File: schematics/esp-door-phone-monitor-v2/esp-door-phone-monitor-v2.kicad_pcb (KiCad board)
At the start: 2 copper layers, 56.8 x 25.7 mm, 47 parts, among them J1 PHONE, J2 PWR_IN, J3 PROGRAM, K1 D3204, Q1 SS8050-G, Q2 SS8050-G, Q3 AO3480, U1 OP07, U2 AMS1117-3.3, U3 ESP-12E

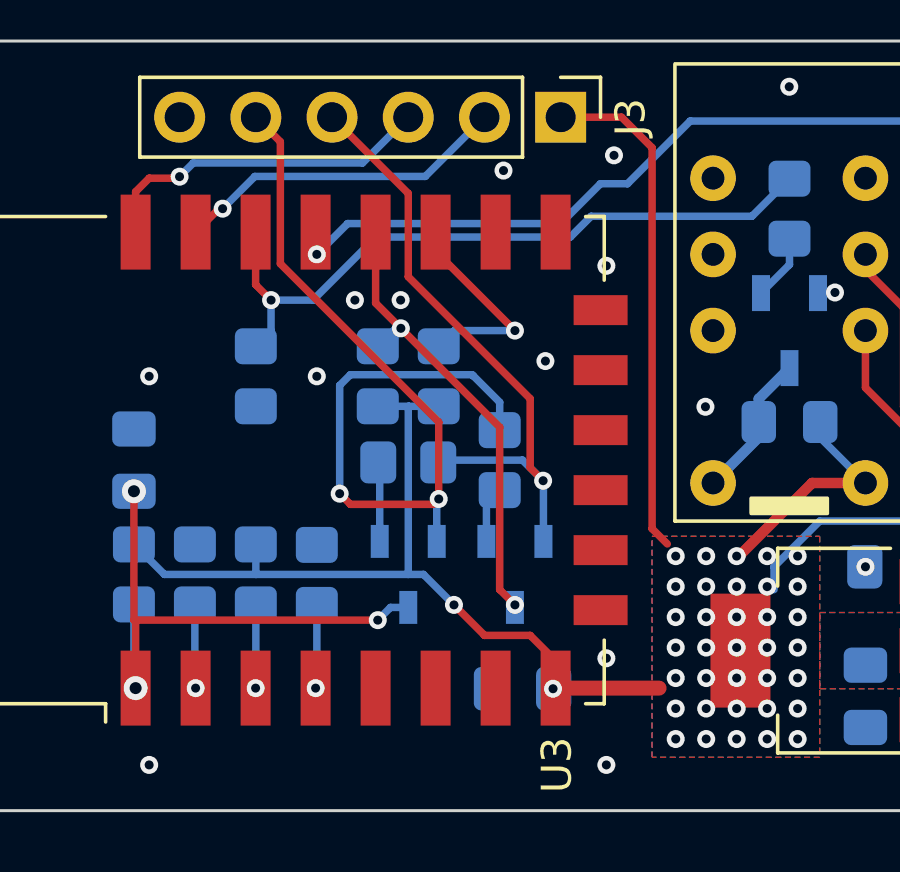
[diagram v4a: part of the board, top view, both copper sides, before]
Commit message: Fix pull-down resistor on GPIO15
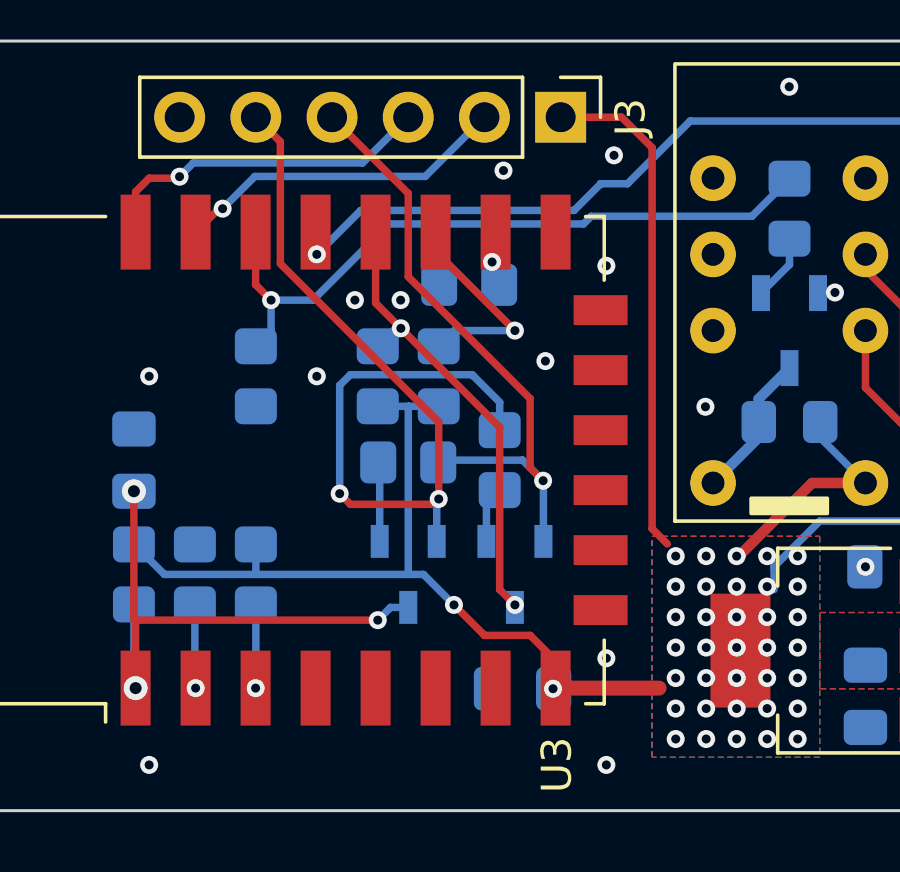
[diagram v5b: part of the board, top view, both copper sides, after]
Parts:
- moved R7 10.9 mm to (128.5, 93.0), turned to 180 degrees
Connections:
- U3 pad 16: unconnected-(U3-Pad16) -> Net-(R7-Pad1)
- U3 pad 4: Net-(R7-Pad1) -> unconnected-(U3-Pad4)
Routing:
- net Net-(R7-Pad1): track 2.79 -> 0.86 mm
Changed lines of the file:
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@@
   (net 19 "unconnected-(U3-Pad13)")
   (net 20 "unconnected-(U3-Pad14)")
-  (net 21 "unconnected-(U3-Pad16)")
+  (net 21 "unconnected-(U3-Pad4)")
   (net 22 "ESP_RINGING_SENSE")
   (net 23 "ESP_MUTE_CTRL")
@@
       (net 7 "ESP_EN") (pinfunction "EN") (pintype "input"))
     (pad "4" smd rect locked (at -7.6 2.5 90) (size 2.5 1) (layers "F.Cu" "F.Paste" "F.Mask")
-      (net 10 "Net-(R7-Pad1)") (pinfunction "GPIO16") (pintype "bidirectional"))
+      (net 21 "unconnected-(U3-Pad4)") (pinfunction "GPIO16") (pintype "bidirectional"))
     (pad "5" smd rect locked (at -7.6 4.5 90) (size 2.5 1) (layers "F.Cu" "F.Paste" "F.Mask")
       (net 12 "unconnected-(U3-Pad5)") (pinfunction "GPIO14") (pintype "bidirectional"))
@@
       (net 2 "GND") (pinfunction "GND") (pintype "power_in"))
     (pad "16" smd rect locked (at 7.6 8.5 90) (size 2.5 1) (layers "F.Cu" "F.Paste" "F.Mask")
-      (net 21 "unconnected-(U3-Pad16)") (pinfunction "GPIO15") (pintype "bidirectional"))
+      (net 10 "Net-(R7-Pad1)") (pinfunction "GPIO15") (pintype "bidirectional"))
     (pad "17" smd rect locked (at 7.6 6.5 90) (size 2.5 1) (layers "F.Cu" "F.Paste" "F.Mask")
       (net 11 "Net-(R8-Pad2)") (pinfunction "GPIO2") (pintype "bidirectional"))
@@
     (property "Sheetname" "")
     (attr smd)
-    (fp_text reference "R6" (at 3.556 0 90) (layer "B.SilkS")
+    (fp_text reference "R6" (at 1.27 -1.778 90) (layer "B.SilkS")
       (effects (font (size 1 1) (thickness 0.15)) (justify mirror))
     )
@@
     (property "Sheetname" "")
     (attr smd)
-    (fp_text reference "R8" (at 3.556 0 90) (layer "B.SilkS")
+    (fp_text reference "R8" (at 0.762 1.778 90) (layer "B.SilkS")
       (effects (font (size 1 1) (thickness 0.15)) (justify mirror))
     )
@@
   )
   (footprint "Resistor_SMD:R_0805_2012Metric_Pad1.20x1.40mm_HandSolder" (layer "B.Cu")
-    (at 123.444 102.632 90)
-    (descr "Resistor SMD 0805 (2012 Metric), square (rectangular) end terminal, IPC_7351 nominal with elongated pad for handsoldering. (Body size source: IPC-SM-782 page 72, https://www.pcb-3d.com/wordpress/wp-content/uploads/ipc-sm-782a_amendment_1_and_2.pdf), generated with kicad-footprint-generator")
-    (tags "resistor handsolder")
-    (property "Sheetfile" "esp-door-phone-monitor-v2.kicad_sch")
-    (property "Sheetname" "")
-    (attr smd)
-    (fp_text reference "R7" (at -2.778 0 90) (layer "B.SilkS")
-      (effects (font (size 1 1) (thickness 0.15)) (justify mirror))
-    )
-    (fp_text value "10k" (at 0 -1.65 90) (layer "B.Fab")
-      (effects (font (size 1 1) (thickness 0.15)) (justify mirror))
-    )
-    (fp_text user "${REFERENCE}" (at 0 0 90) (layer "B.Fab")
+    (at 128.524 92.964 180)
+    (descr "Resistor SMD 0805 (2012 Metric), square (rectangular) end terminal, IPC_7351 nominal with elongated pad for handsoldering. (Body size source: IPC-SM-782 page 72, https://www.pcb-3d.com/wordpress/wp-content/uploads/ipc-sm-782a_amendment_1_and_2.pdf), generated with kicad-footprint-generator")
+    (tags "resistor handsolder")
+    (property "Sheetfile" "esp-door-phone-monitor-v2.kicad_sch")
+    (property "Sheetname" "")
+    (attr smd)
+    (fp_text reference "R7" (at -3.048 0) (layer "B.SilkS")
+      (effects (font (size 1 1) (thickness 0.15)) (justify mirror))
+    )
+    (fp_text value "10k" (at 0 -1.65) (layer "B.Fab")
+      (effects (font (size 1 1) (thickness 0.15)) (justify mirror))
+    )
+    (fp_text user "${REFERENCE}" (at 0 0) (layer "B.Fab")
       (effects (font (size 0.5 0.5) (thickness 0.08)) (justify mirror))
     )
@@
     (fp_line (start 1 -0.625) (end -1 -0.625) (layer "B.Fab") (width 0.1))
     (fp_line (start 1 0.625) (end 1 -0.625) (layer "B.Fab") (width 0.1))
-    (pad "1" smd roundrect locked (at -1 0 90) (size 1.2 1.4) (layers "B.Cu" "B.Paste" "B.Mask") (roundrect_rratio 0.2083333333)
+    (pad "1" smd roundrect locked (at -1 0 180) (size 1.2 1.4) (layers "B.Cu" "B.Paste" "B.Mask") (roundrect_rratio 0.2083333333)
       (net 10 "Net-(R7-Pad1)") (pintype "passive"))
-    (pad "2" smd roundrect locked (at 1 0 90) (size 1.2 1.4) (layers "B.Cu" "B.Paste" "B.Mask") (roundrect_rratio 0.2083333333)
+    (pad "2" smd roundrect locked (at 1 0 180) (size 1.2 1.4) (layers "B.Cu" "B.Paste" "B.Mask") (roundrect_rratio 0.2083333333)
       (net 2 "GND") (pintype "passive"))
     (model "${KICAD6_3DMODEL_DIR}/Resistor_SMD.3dshapes/R_0805_2012Metric.wrl"
@@
   (segment (start 126.075625 94.412375) (end 125.476 95.012) (width 0.25) (layer "B.Cu") (net 9))
   (segment (start 126.246003 94.412375) (end 126.075625 94.412375) (width 0.25) (layer "B.Cu") (net 9))
-  (via (at 123.404 106.406) (size 0.6) (drill 0.3) (layers "F.Cu" "B.Cu") (net 10))
-  (segment (start 123.444 106.366) (end 123.404 106.406) (width 0.25) (layer "B.Cu") (net 10))
-  (segment (start 123.444 103.632) (end 123.444 106.366) (width 0.25) (layer "B.Cu") (net 10))
+  (via (at 129.286 92.202) (size 0.6) (drill 0.3) (layers "F.Cu" "B.Cu") (net 10))
+  (segment (start 129.524 92.964) (end 129.524 92.44) (width 0.25) (layer "B.Cu") (net 10))
+  (segment (start 129.524 92.44) (end 129.286 92.202) (width 0.25) (layer "B.Cu") (net 10))
   (segment (start 127.404 91.206) (end 127.404 91.844) (width 0.25) (layer "F.Cu") (net 11))
   (segment (start 127.404 91.844) (end 130.048 94.488) (width 0.25) (layer "F.Cu") (net 11))
@@
   (segment (start 130.048 94.488) (end 128.032 94.488) (width 0.25) (layer "B.Cu") (net 11))
   (via (at 123.444 91.948) (size 0.6) (drill 0.3) (layers "F.Cu" "B.Cu") (net 22))
+  (segment (start 132.898489 89.59348) (end 132.898489 89.605511) (width 0.25) (layer "B.Cu") (net 22))
   (segment (start 146.787 91.694) (end 146.787 89.669) (width 0.25) (layer "B.Cu") (net 22))
+  (segment (start 132.898489 89.605511) (end 132.02152 90.48248) (width 0.25) (layer "B.Cu") (net 22))
   (segment (start 146.78 89.122) (end 145.161 87.503) (width 0.25) (layer "B.Cu") (net 22))
-  (segment (start 124.472031 90.919969) (end 123.444 91.948) (width 0.25) (layer "B.Cu") (net 22))
-  (segment (start 146.78 89.662) (end 146.78 89.122) (width 0.25) (layer "B.Cu") (net 22))
-  (segment (start 132.898489 89.59348) (end 131.572 90.919969) (width 0.25) (layer "B.Cu") (net 22))
+  (segment (start 132.02152 90.48248) (end 124.90952 90.48248) (width 0.25) (layer "B.Cu") (net 22))
+  (segment (start 145.161 87.503) (end 135.89 87.503) (width 0.25) (layer "B.Cu") (net 22))
   (segment (start 133.79952 89.59348) (end 132.898489 89.59348) (width 0.25) (layer "B.Cu") (net 22))
+  (segment (start 124.90952 90.48248) (end 123.444 91.948) (width 0.25) (layer "B.Cu") (net 22))
   (segment (start 135.89 87.503) (end 133.79952 89.59348) (width 0.25) (layer "B.Cu") (net 22))
   (segment (start 146.787 89.669) (end 146.78 89.662) (width 0.25) (layer "B.Cu") (net 22))
-  (segment (start 145.161 87.503) (end 135.89 87.503) (width 0.25) (layer "B.Cu") (net 22))
-  (segment (start 131.572 90.919969) (end 124.472031 90.919969) (width 0.25) (layer "B.Cu") (net 22))
+  (segment (start 146.78 89.662) (end 146.78 89.122) (width 0.25) (layer "B.Cu") (net 22))
   (segment (start 121.404 91.206) (end 121.404 92.956) (width 0.25) (layer "F.Cu") (net 23))
   (segment (start 121.404 92.956) (end 121.92 93.472) (width 0.25) (layer "F.Cu") (net 23))
   (via (at 121.92 93.472) (size 0.6) (drill 0.3) (layers "F.Cu" "B.Cu") (net 23))
-  (segment (start 132.588 90.678) (end 131.896511 91.369489) (width 0.25) (layer "B.Cu") (net 23))
+  (segment (start 121.92 94.504) (end 121.412 95.012) (width 0.25) (layer "B.Cu") (net 23))
+  (segment (start 125.857 90.932) (end 123.317 93.472) (width 0.25) (layer "B.Cu") (net 23))
+  (segment (start 139.201 89.424) (end 137.947 90.678) (width 0.25) (layer "B.Cu") (net 23))
+  (segment (start 132.334 90.932) (end 125.857 90.932) (width 0.25) (layer "B.Cu") (net 23))
+  (segment (start 132.588 90.678) (end 132.334 90.932) (width 0.25) (layer "B.Cu") (net 23))
   (segment (start 137.947 90.678) (end 132.588 90.678) (width 0.25) (layer "B.Cu") (net 23))
-  (segment (start 121.92 94.504) (end 121.412 95.012) (width 0.25) (layer "B.Cu") (net 23))
   (segment (start 123.317 93.472) (end 121.92 93.472) (width 0.25) (layer "B.Cu") (net 23))
-  (segment (start 125.419511 91.369489) (end 123.317 93.472) (width 0.25) (layer "B.Cu") (net 23))
-  (segment (start 131.896511 91.369489) (end 125.419511 91.369489) (width 0.25) (layer "B.Cu") (net 23))
-  (segment (start 139.201 89.424) (end 137.947 90.678) (width 0.25) (layer "B.Cu") (net 23))
   (segment (start 121.92 93.472) (end 121.92 94.504) (width 0.25) (layer "B.Cu") (net 23))
   (segment (start 120.304498 90.424) (end 120.186 90.424) (width 0.25) (layer "F.Cu") (net 24))

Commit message: Fix the reversed flyback diode D4
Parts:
- turned D4 to 180 degrees
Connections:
- D4 pad 1: Net-(D4-Pad1) -> VDD
- D4 pad 2: VDD -> Net-(K1-Pad10)
- K1 pad 10: Net-(D4-Pad1) -> Net-(K1-Pad10)
- Q3 pad 3: Net-(D4-Pad1) -> Net-(K1-Pad10)
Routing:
- net Net-(K1-Pad10): track 0.00 -> 4.89 mm
- net Net-(D4-Pad1): track 4.89 -> 0.00 mm
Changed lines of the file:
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@@
   (net 42 "unconnected-(U1-Pad5)")
   (net 43 "unconnected-(U1-Pad8)")
-  (net 44 "Net-(D4-Pad1)")
+  (net 44 "Net-(K1-Pad10)")
   (net 45 "SPEAKER_GND_OUT")
   (net 46 "unconnected-(K1-Pad5)")
@@
       (net 49 "unconnected-(K1-Pad8)") (pintype "passive"))
     (pad "10" thru_hole circle (at -5.08 -2.54 90) (size 1.524 1.524) (drill 0.762) (layers *.Cu *.Mask)
-      (net 44 "Net-(D4-Pad1)") (pintype "passive"))
+      (net 44 "Net-(K1-Pad10)") (pintype "passive"))
   )
   (footprint "Connector_Wire:SolderWire-0.5sqmm_1x03_P4.6mm_D0.9mm_OD2.1mm" (layer "F.Cu")
@@
       (net 2 "GND") (pintype "unspecified"))
     (pad "3" smd rect locked (at 1.25 0 180) (size 0.6 1.2) (layers "B.Cu" "B.Paste" "B.Mask")
-      (net 44 "Net-(D4-Pad1)") (pintype "unspecified"))
+      (net 44 "Net-(K1-Pad10)") (pintype "unspecified"))
     (model "C:/SamacSys_PCB_Library/KiCad/SamacSys_Parts.3dshapes/AO3401A.wrl"
       (offset (xyz 0 0 0))
@@
   )
   (footprint "Diode_SMD:D_0805_2012Metric_Pad1.15x1.40mm_HandSolder" (layer "B.Cu")
-    (at 139.201 97.536)
+    (at 139.201 97.536 180)
     (descr "Diode SMD 0805 (2012 Metric), square (rectangular) end terminal, IPC_7351 nominal, (Body size source: https://docs.google.com/spreadsheets/d/1BsfQQcO9C6DZCsRaXUlFlo91Tg2WpOkGARC1WS5S8t0/edit?usp=sharing), generated with kicad-footprint-generator")
     (tags "diode handsolder")
@@
     (property "Sheetname" "")
     (attr smd)
-    (fp_text reference "D4" (at -0.009 1.778) (layer "B.SilkS")
+    (fp_text reference "D4" (at -0.0164 -1.8288) (layer "B.SilkS")
       (effects (font (size 1 1) (thickness 0.15)) (justify mirror))
     )
@@
     (fp_line (start -0.7 0.6) (end -1 0.3) (layer "B.Fab") (width 0.1))
     (fp_line (start -1 0.3) (end -1 -0.6) (layer "B.Fab") (width 0.1))
-    (pad "1" smd roundrect locked (at -1.025 0) (size 1.15 1.4) (layers "B.Cu" "B.Paste" "B.Mask") (roundrect_rratio 0.2173913043)
-      (net 44 "Net-(D4-Pad1)") (pinfunction "K") (pintype "passive"))
-    (pad "2" smd roundrect locked (at 1.025 0) (size 1.15 1.4) (layers "B.Cu" "B.Paste" "B.Mask") (roundrect_rratio 0.2173913043)
-      (net 1 "VDD") (pinfunction "A") (pintype "passive"))
+    (pad "1" smd roundrect locked (at -1.025 0 180) (size 1.15 1.4) (layers "B.Cu" "B.Paste" "B.Mask") (roundrect_rratio 0.2173913043)
+      (net 1 "VDD") (pinfunction "K") (pintype "passive"))
+    (pad "2" smd roundrect locked (at 1.025 0 180) (size 1.15 1.4) (layers "B.Cu" "B.Paste" "B.Mask") (roundrect_rratio 0.2173913043)
+      (net 44 "Net-(K1-Pad10)") (pinfunction "A") (pintype "passive"))
     (model "${KICAD6_3DMODEL_DIR}/Diode_SMD.3dshapes/D_0805_2012Metric.wrl"
       (offset (xyz 0 0 0))
